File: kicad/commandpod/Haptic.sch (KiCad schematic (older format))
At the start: 1 part

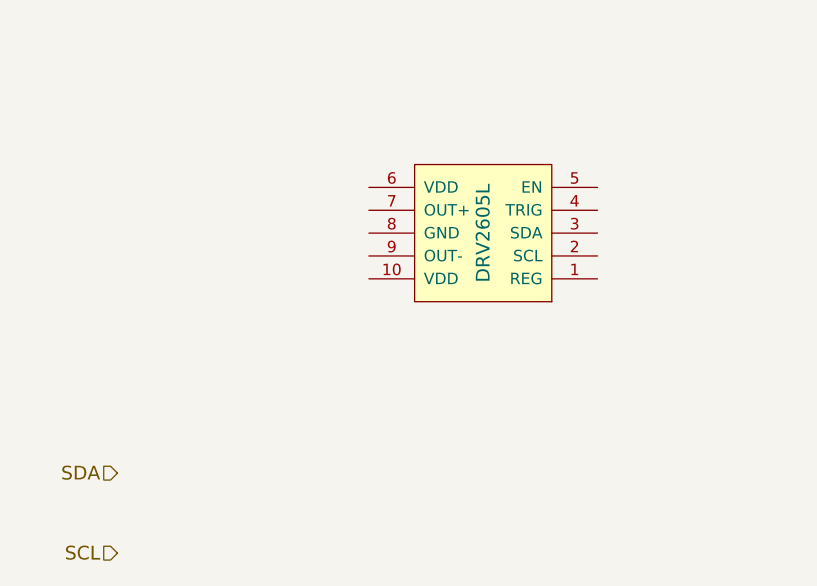
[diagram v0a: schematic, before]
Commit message: Annotated schematics
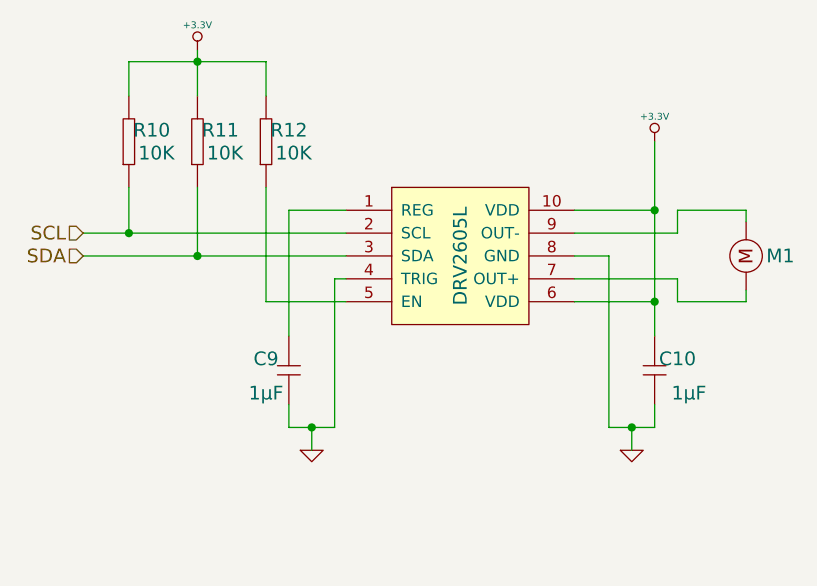
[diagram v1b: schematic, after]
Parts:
- added C10, C9: GENERIC_CAPACITOR, ~, symbol GENERIC_CAPACITOR
- added M1: MOTOR, ~, symbol MOTOR
- added R10, R11, R12: GENERIC_RESISTOR, ~, symbol GENERIC_RESISTOR
- gave numbers to parts that had none: 1
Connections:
- net SCL: now also DRV1.2 (SCL), R10.2
- net SDA: now also DRV1.3 (SDA), R11.2
- net at DRV1.1 (REG): now also C9.2
- net +3.3V: now reaches DRV1.10 (VDD)
- net +3.3V: now also DRV1.6 (VDD), C10.2, R10.1, R11.1, R12.1
- net GND: now reaches DRV1.4 (TRIG)
- net GND: now also DRV1.8 (GND), C10.1, C9.1
- net at DRV1.5 (EN): now also R12.2
- net at DRV1.7 (OUT+): now also M1.1
- net at DRV1.9 (OUT-): now also M1.2
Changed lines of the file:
@@
 $EndDescr
 $Comp
-L DRV2605L DRV?
+L DRV2605L DRV1
 U 1 1 56D8221C
-P 5650 3800
-F 0 "DRV?" H 5450 3450 60  0001 C CNN
-F 1 "DRV2605L" V 5650 3800 60  0000 C CNN
-F 2 "" H 5700 3900 60  0000 C CNN
-F 3 "" H 5700 3900 60  0000 C CNN
-F 4 "DRV2605L" H 5950 4200 60  0001 C CNN "Part #"
-	1    5650 3800
-	-1   0    0    1
-$EndComp
-Text HLabel 4050 4850 0    60   Input ~ 0
+P 5550 3900
+F 0 "DRV1" H 5350 3550 60  0001 C CNN
+F 1 "DRV2605L" V 5550 3900 60  0000 C CNN
+F 2 "" H 5600 4000 60  0000 C CNN
+F 3 "" H 5600 4000 60  0000 C CNN
+F 4 "DRV2605L" H 5850 4300 60  0001 C CNN "Part #"
+	1    5550 3900
+	1    0    0    -1
+$EndComp
+Text HLabel 3900 3900 0    60   Input ~ 0
 SDA
-Text HLabel 4050 5200 0    60   Input ~ 0
+Text HLabel 3900 3800 0    60   Input ~ 0
 SCL
+$Comp
+L +3.3V #PWR035
+U 1 1 56D83A70
+P 6400 3400
+F 0 "#PWR035" H 6400 3360 30  0001 C CNN
+F 1 "+3.3V" H 6400 3510 30  0000 C CNN
+F 2 "" H 6400 3400 60  0000 C CNN
+F 3 "" H 6400 3400 60  0000 C CNN
+	1    6400 3400
+	1    0    0    -1
+$EndComp
+$Comp
+L GND #PWR036
+U 1 1 56D83A7F
+P 6300 4750
+F 0 "#PWR036" H 6300 4750 30  0001 C CNN
+F 1 "GND" H 6300 4680 30  0001 C CNN
+F 2 "" H 6300 4750 60  0000 C CNN
+F 3 "" H 6300 4750 60  0000 C CNN
+	1    6300 4750
+	1    0    0    -1
+$EndComp
+Wire Wire Line
+	6400 3400 6400 4250
+Connection ~ 6400 3700
+$Comp
+L MOTOR M1
+U 1 1 56D83AA1
+P 6800 3900
+F 0 "M1" V 6800 3750 60  0000 C CNN
+F 1 "MOTOR" H 6800 4050 60  0001 C CNN
+F 2 "~" H 6800 3900 60  0000 C CNN
+F 3 "~" H 6800 3900 60  0000 C CNN
+	1    6800 3900
+	0    -1   -1   0
+$EndComp
+Wire Wire Line
+	6800 3700 6800 3750
+Wire Wire Line
+	6800 4100 6800 4050
+Wire Wire Line
+	6050 3700 6400 3700
+Wire Wire Line
+	6400 4100 6050 4100
+Wire Wire Line
+	6050 4000 6500 4000
+Wire Wire Line
+	6500 4000 6500 4100
+Wire Wire Line
+	6500 4100 6800 4100
+Wire Wire Line
+	6050 3800 6500 3800
+Wire Wire Line
+	6500 3800 6500 3700
+Wire Wire Line
+	6500 3700 6800 3700
+$Comp
+L GND #PWR037
+U 1 1 56D83C30
+P 4900 4750
+F 0 "#PWR037" H 4900 4750 30  0001 C CNN
+F 1 "GND" H 4900 4680 30  0001 C CNN
+F 2 "" H 4900 4750 60  0000 C CNN
+F 3 "" H 4900 4750 60  0000 C CNN
+	1    4900 4750
+	1    0    0    -1
+$EndComp
+Wire Wire Line
+	3900 3800 5050 3800
+Wire Wire Line
+	3900 3900 5050 3900
+$Comp
+L GENERIC_RESISTOR R12
+U 1 1 56D83C75
+P 4700 3400
+F 0 "R12" V 4750 3300 60  0000 C CNN
+F 1 "GENERIC_RESISTOR" H 4740 3180 60  0001 C CNN
+F 2 "~" H 4650 3150 60  0000 C CNN
+F 3 "~" H 4650 3150 60  0000 C CNN
+F 4 "10K" V 4650 3200 60  0000 L CNN "Resistance"
+F 5 "~" H 4910 3480 60  0001 C CNN "Part #"
+	1    4700 3400
+	0    -1   -1   0
+$EndComp
+$Comp
+L GENERIC_RESISTOR R11
+U 1 1 56D83CF8
+P 4400 3400
+F 0 "R11" V 4450 3300 60  0000 C CNN
+F 1 "GENERIC_RESISTOR" H 4440 3180 60  0001 C CNN
+F 2 "~" H 4350 3150 60  0000 C CNN
+F 3 "~" H 4350 3150 60  0000 C CNN
+F 4 "10K" V 4350 3200 60  0000 L CNN "Resistance"
+F 5 "~" H 4610 3480 60  0001 C CNN "Part #"
+	1    4400 3400
+	0    -1   -1   0
+$EndComp
+$Comp
+L GENERIC_RESISTOR R10
+U 1 1 56D83D00
+P 4100 3400
+F 0 "R10" V 4150 3300 60  0000 C CNN
+F 1 "GENERIC_RESISTOR" H 4140 3180 60  0001 C CNN
+F 2 "~" H 4050 3150 60  0000 C CNN
+F 3 "~" H 4050 3150 60  0000 C CNN
+F 4 "10K" V 4050 3200 60  0000 L CNN "Resistance"
+F 5 "~" H 4310 3480 60  0001 C CNN "Part #"
+	1    4100 3400
+	0    -1   -1   0
+$EndComp
+$Comp
+L +3.3V #PWR038
+U 1 1 56D83D16
+P 4400 3000
+F 0 "#PWR038" H 4400 2960 30  0001 C CNN
+F 1 "+3.3V" H 4400 3110 30  0000 C CNN
+F 2 "" H 4400 3000 60  0000 C CNN
+F 3 "" H 4400 3000 60  0000 C CNN
+	1    4400 3000
+	1    0    0    -1
+$EndComp
+Wire Wire Line
+	4100 3200 4100 3050
+Wire Wire Line
+	4100 3050 4700 3050
+Wire Wire Line
+	4400 3000 4400 3200
+Connection ~ 4400 3050
+Wire Wire Line
+	4700 3050 4700 3200
+Wire Wire Line
+	4100 3600 4100 3800
+Connection ~ 4100 3800
+Wire Wire Line
+	4400 3600 4400 3900
+Connection ~ 4400 3900
+Wire Wire Line
+	4700 3600 4700 4100
+Wire Wire Line
+	4700 4100 5050 4100
+$Comp
+L GENERIC_CAPACITOR C9
+U 1 1 56D83E5A
+P 4800 4400
+F 0 "C9" V 4750 4300 60  0000 C CNN
+F 1 "GENERIC_CAPACITOR" H 4810 4200 60  0001 C CNN
+F 2 "~" H 4770 4150 60  0000 C CNN
+F 3 "~" H 4770 4150 60  0000 C CNN
+F 4 "1µF" V 4900 4300 60  0000 C CNN "Capacitance"
+F 5 "~" H 5110 4520 60  0001 C CNN "Part #"
+	1    4800 4400
+	0    1    1    0
+$EndComp
+$Comp
+L GENERIC_CAPACITOR C10
+U 1 1 56D84177
+P 6400 4400
+F 0 "C10" V 6350 4500 60  0000 C CNN
+F 1 "GENERIC_CAPACITOR" H 6410 4200 60  0001 C CNN
+F 2 "~" H 6370 4150 60  0000 C CNN
+F 3 "~" H 6370 4150 60  0000 C CNN
+F 4 "1µF" V 6500 4550 60  0000 C CNN "Capacitance"
+F 5 "~" H 6710 4520 60  0001 C CNN "Part #"
+	1    6400 4400
+	0    1    1    0
+$EndComp
+Wire Wire Line
+	6050 3900 6200 3900
+Wire Wire Line
+	6400 4650 6400 4550
+Connection ~ 6400 4100
+Wire Wire Line
+	6200 3900 6200 4650
+Wire Wire Line
+	6200 4650 6400 4650
+Wire Wire Line
+	6300 4650 6300 4750
+Connection ~ 6300 4650
+Wire Wire Line
+	4800 4250 4800 3700
+Wire Wire Line
+	4800 3700 5050 3700
+Wire Wire Line
+	4800 4550 4800 4650
+Wire Wire Line
+	4800 4650 5000 4650
+Wire Wire Line
+	5000 4650 5000 4000
+Wire Wire Line
+	5000 4000 5050 4000
+Wire Wire Line
+	4900 4750 4900 4650
+Connection ~ 4900 4650
 $EndSCHEMATC
